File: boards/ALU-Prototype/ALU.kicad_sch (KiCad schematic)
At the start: 13 parts

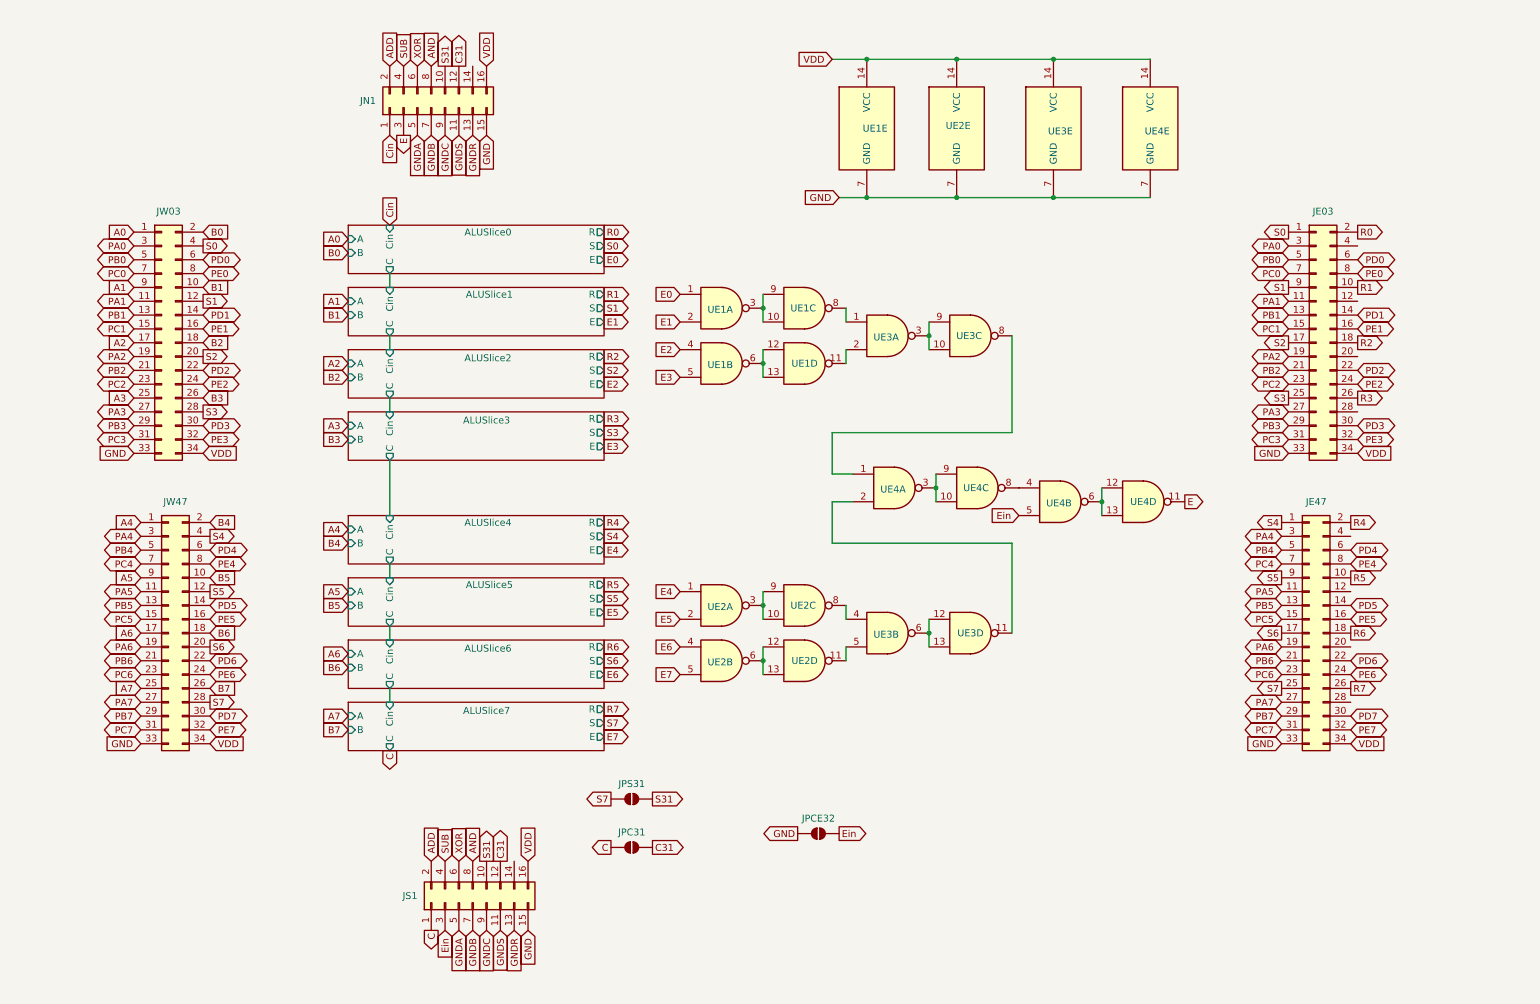
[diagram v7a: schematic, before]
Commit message: SetBit0 and routing of the PCB
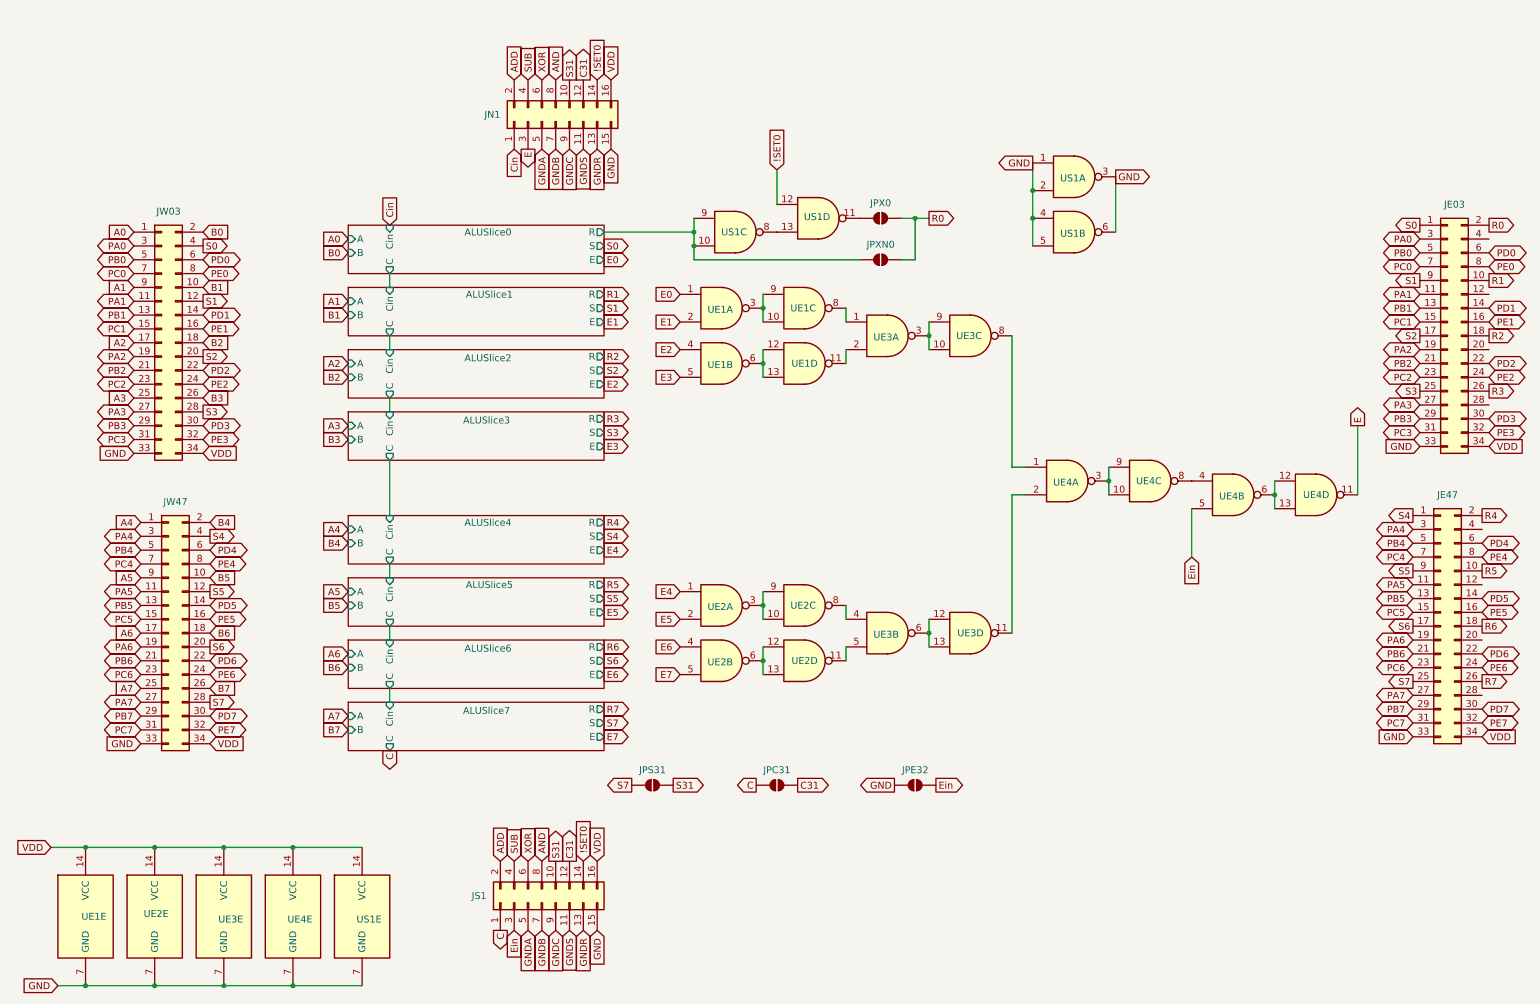
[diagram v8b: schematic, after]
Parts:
- added JPX0, JPXN0: ~, Jumper:SolderJumper-2_P1.3mm_Open_Pad1.0x1.5mm, symbol Jumper:SolderJumper_2_Open
- added US1: ~, Package_SO:TSSOP-14_4.4x5mm_P0.65mm, symbol 74xx:7400
- JPC31, JPS31: value SolderJumper_2_Open -> ~
- JPE32: renamed from JPCE32; value SolderJumper_2_Open -> ~
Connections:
- net GND: now also US1.1, US1.2, US1.3, US1.4, US1.5, US1.6, US1.7 (GND)
- net R0: now also JPX0.2 (B), JPXN0.2 (B)
- net VDD: now also US1.14 (VCC)
- net !SET0: now reaches JN1.14 (Pin_14)
- net !SET0: now also JS1.14 (Pin_14), US1.12
- new net: US1.13, US1.8
- new net: JPX0.1 (A), US1.11
- new net ALUSlice0/R: JPXN0.1 (A), US1.10, US1.9
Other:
- moved on the sheet: JE03, JE47, JN1, JPC31, JPE32, JPS31, JS1, UE1E, UE2E, UE3E, UE4A, UE4B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
